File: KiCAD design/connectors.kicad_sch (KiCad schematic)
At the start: 8 parts, among them J201 Conn_02x19_Odd_Even, J202 Conn_01x03_Female, J203 Conn_01x03_Female, J204 Conn_02x19_Odd_Even, J205 JST BATTERY, J206 JST SENS TOF 2, J207 Conn_01x06_Female, J208 JST SENS TOF 1

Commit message: add of footprint and nucleo as a reference
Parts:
- J201, J204: footprint (none) -> Connector_JST:JST_PUD_B38B-PUDSS_2x19_P2.00mm_Vertical
- J202, J203: footprint (none) -> Connector_JST:JST_XH_B3B-XH-A_1x03_P2.50mm_Vertical
- J207: footprint (none) -> Connector_JST:JST_XH_B6B-XH-A_1x06_P2.50mm_Vertical
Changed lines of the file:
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@@
       (effects (font (size 1.27 1.27)) (justify left))
     )
-    (property "Footprint" "" (id 2) (at 66.04 157.48 0)
+    (property "Footprint" "Connector_JST:JST_XH_B3B-XH-A_1x03_P2.50mm_Vertical" (id 2) (at 66.04 157.48 0)
       (effects (font (size 1.27 1.27)) hide)
     )
@@
     (property "Reference" "J204" (id 0) (at 113.03 26.1112 0))
     (property "Value" "Conn_02x19_Odd_Even" (id 1) (at 113.03 28.6512 0))
-    (property "Footprint" "" (id 2) (at 111.76 55.88 0)
+    (property "Footprint" "Connector_JST:JST_PUD_B38B-PUDSS_2x19_P2.00mm_Vertical" (id 2) (at 111.76 55.88 0)
       (effects (font (size 1.27 1.27)) hide)
     )
@@
     (property "Reference" "J201" (id 0) (at 44.45 26.1112 0))
     (property "Value" "Conn_02x19_Odd_Even" (id 1) (at 44.45 28.6512 0))
-    (property "Footprint" "" (id 2) (at 43.18 55.88 0)
+    (property "Footprint" "Connector_JST:JST_PUD_B38B-PUDSS_2x19_P2.00mm_Vertical" (id 2) (at 43.18 55.88 0)
       (effects (font (size 1.27 1.27)) hide)
     )
@@
       (effects (font (size 1.27 1.27)) (justify left))
     )
-    (property "Footprint" "" (id 2) (at 66.04 137.16 0)
+    (property "Footprint" "Connector_JST:JST_XH_B3B-XH-A_1x03_P2.50mm_Vertical" (id 2) (at 66.04 137.16 0)
       (effects (font (size 1.27 1.27)) hide)
     )
@@
       (effects (font (size 1.27 1.27)) (justify left))
     )
-    (property "Footprint" "" (id 2) (at 225.425 138.43 0)
-      (effects (font (size 1.27 1.27)) hide)
-    )
+    (property "Footprint" "Connector_JST:JST_XH_B6B-XH-A_1x06_P2.50mm_Vertical" (id 2) (at 225.425 138.43 0)
+      (effects (font (size 1.27 1.27)) hide)
+    )

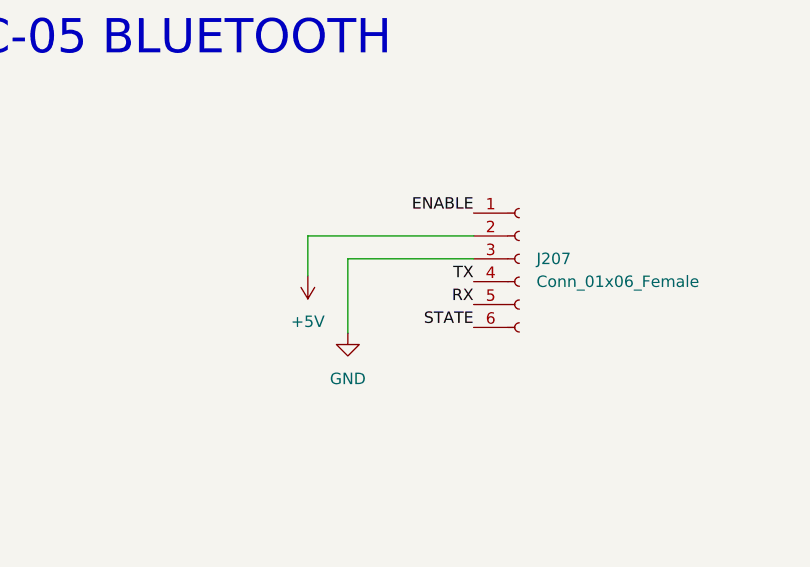
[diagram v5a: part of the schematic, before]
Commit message: add BLUETOOTH_*X labels to bluetooth module
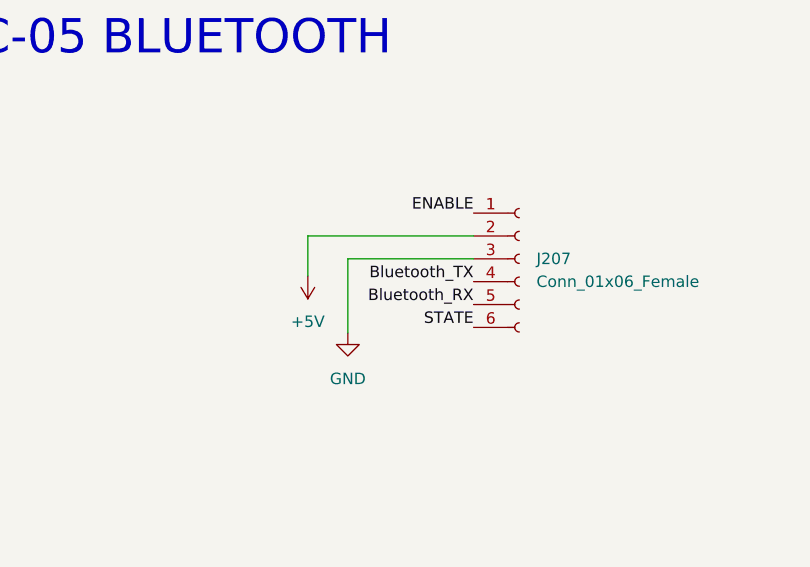
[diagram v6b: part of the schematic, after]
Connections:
- net RX is gone; now on net Bluetooth_RX: J207.5 (Pin_5)
- net TX is gone; now on net Bluetooth_TX: J207.4 (Pin_4)
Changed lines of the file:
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@@
     (effects (font (size 1.27 1.27)) (justify right bottom))
   )
-  (label "TX" (at 220.345 140.97 180)
+  (label "Bluetooth_TX" (at 220.345 140.97 180)
     (effects (font (size 1.27 1.27)) (justify right bottom))
   )
@@
     (effects (font (size 1.27 1.27) (thickness 0.254) bold) (justify right bottom))
   )
-  (label "RX" (at 220.345 143.51 180)
+  (label "Bluetooth_RX" (at 220.345 143.51 180)
     (effects (font (size 1.27 1.27)) (justify right bottom))
   )

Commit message: added PurchaseLoc and Price to most of the main components, leds, resistors, capacitors, switch, bluetooth missing
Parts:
- J201, J204: Price (none) -> 2.11; PurchaseLoc (none) -> https://www.digikey.fi/en/products/detail/sullins-connector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
- J202, J203: Price (none) -> 0.24; PurchaseLoc (none) -> https://www.digikey.fi/en/products/detail/molex/0022035035/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
- J206, J207, J208: Price (none) -> 0.27; PurchaseLoc (none) -> https://www.digikey.fi/en/products/detail/assmann-wsw-compo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
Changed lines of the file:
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@@
+      (effects (font (size 1.27 1.27)) hide)
+    )
+    (property "PurchaseLoc" "https://www.digikey.fi/en/products/detail/molex/0022035035/403302?s=N4IgTCBcDa5gDAZgKxOSAugXyA" (id 5) (at 66.04 157.48 0)
+      (effects (font (size 1.27 1.27)) hide)
+    )
+    (property "Price" "0.24" (id 4) (at 66.04 157.48 0)
       (effects (font (size 1.27 1.27)) hide)
     )
@@
     )
     (property "Datasheet" "~" (id 3) (at 111.76 55.88 0)
+      (effects (font (size 1.27 1.27)) hide)
+    )
+    (property "PurchaseLoc" "https://www.digikey.fi/en/products/detail/sullins-connector-solutions/PPPC192LFBN-RC/810258" (id 4) (at 111.76 55.88 0)
+      (effects (font (size 1.27 1.27)) hide)
+    )
+    (property "Price" "2.11" (id 5) (at 111.76 55.88 0)
       (effects (font (size 1.27 1.27)) hide)
     )
@@
       (effects (font (size 1.27 1.27)) hide)
     )
+    (property "PurchaseLoc" "https://www.digikey.fi/en/products/detail/assmann-wsw-components/AW-127-06-G-T/16906693" (id 4) (at 203.2 58.42 0)
+      (effects (font (size 1.27 1.27)) hide)
+    )
+    (property "Price" "0.27" (id 5) (at 203.2 58.42 0)
+      (effects (font (size 1.27 1.27)) hide)
+    )
     (pin "1")
     (pin "2")
@@
     )
     (property "Datasheet" "~" (id 3) (at 43.18 55.88 0)
+      (effects (font (size 1.27 1.27)) hide)
+    )
+    (property "PurchaseLoc" "https://www.digikey.fi/en/products/detail/sullins-connector-solutions/PPPC192LFBN-RC/810258" (id 4) (at 43.18 55.88 0)
+      (effects (font (size 1.27 1.27)) hide)
+    )
+    (property "Price" "2.11" (id 5) (at 43.18 55.88 0)
       (effects (font (size 1.27 1.27)) hide)
     )
@@
       (effects (font (size 1.27 1.27)) hide)
     )
+    (property "PurchaseLoc" "https://www.digikey.fi/en/products/detail/assmann-wsw-components/AW-127-06-G-T/16906693" (id 5) (at 257.175 59.055 0)
+      (effects (font (size 1.27 1.27)) hide)
+    )
+    (property "Price" "0.27" (id 5) (at 257.175 59.055 0)
+      (effects (font (size 1.27 1.27)) hide)
+    )
     (pin "1")
     (pin "2")
@@
       (effects (font (size 1.27 1.27)) hide)
     )
+    (property "PurchaseLoc" "https://www.digikey.fi/en/products/detail/molex/0022035035/403302?s=N4IgTCBcDa5gDAZgKxOSAugXyA" (id 4) (at 66.04 137.16 0)
+      (effects (font (size 1.27 1.27)) hide)
+    )
+    (property "Price" "0.24" (id 5) (at 66.04 137.16 0)
+      (effects (font (size 1.27 1.27)) hide)
+    )
     (pin "1")
     (pin "2")
@@
       (effects (font (size 1.27 1.27)) hide)
     )
+    (property "PurchaseLoc" "https://www.digikey.fi/en/products/detail/assmann-wsw-components/AW-127-06-G-T/16906693" (id 4) (at 225.425 138.43 0)
+      (effects (font (size 1.27 1.27)) hide)
+    )
+    (property "Price" "0.27" (id 5) (at 225.425 138.43 0)
+      (effects (font (size 1.27 1.27)) hide)
+    )
